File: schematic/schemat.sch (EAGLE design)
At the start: 69 parts, among them IC1 TB6612FNG, IC2 LM339D, IC3 7806DT, Q1 16MHz

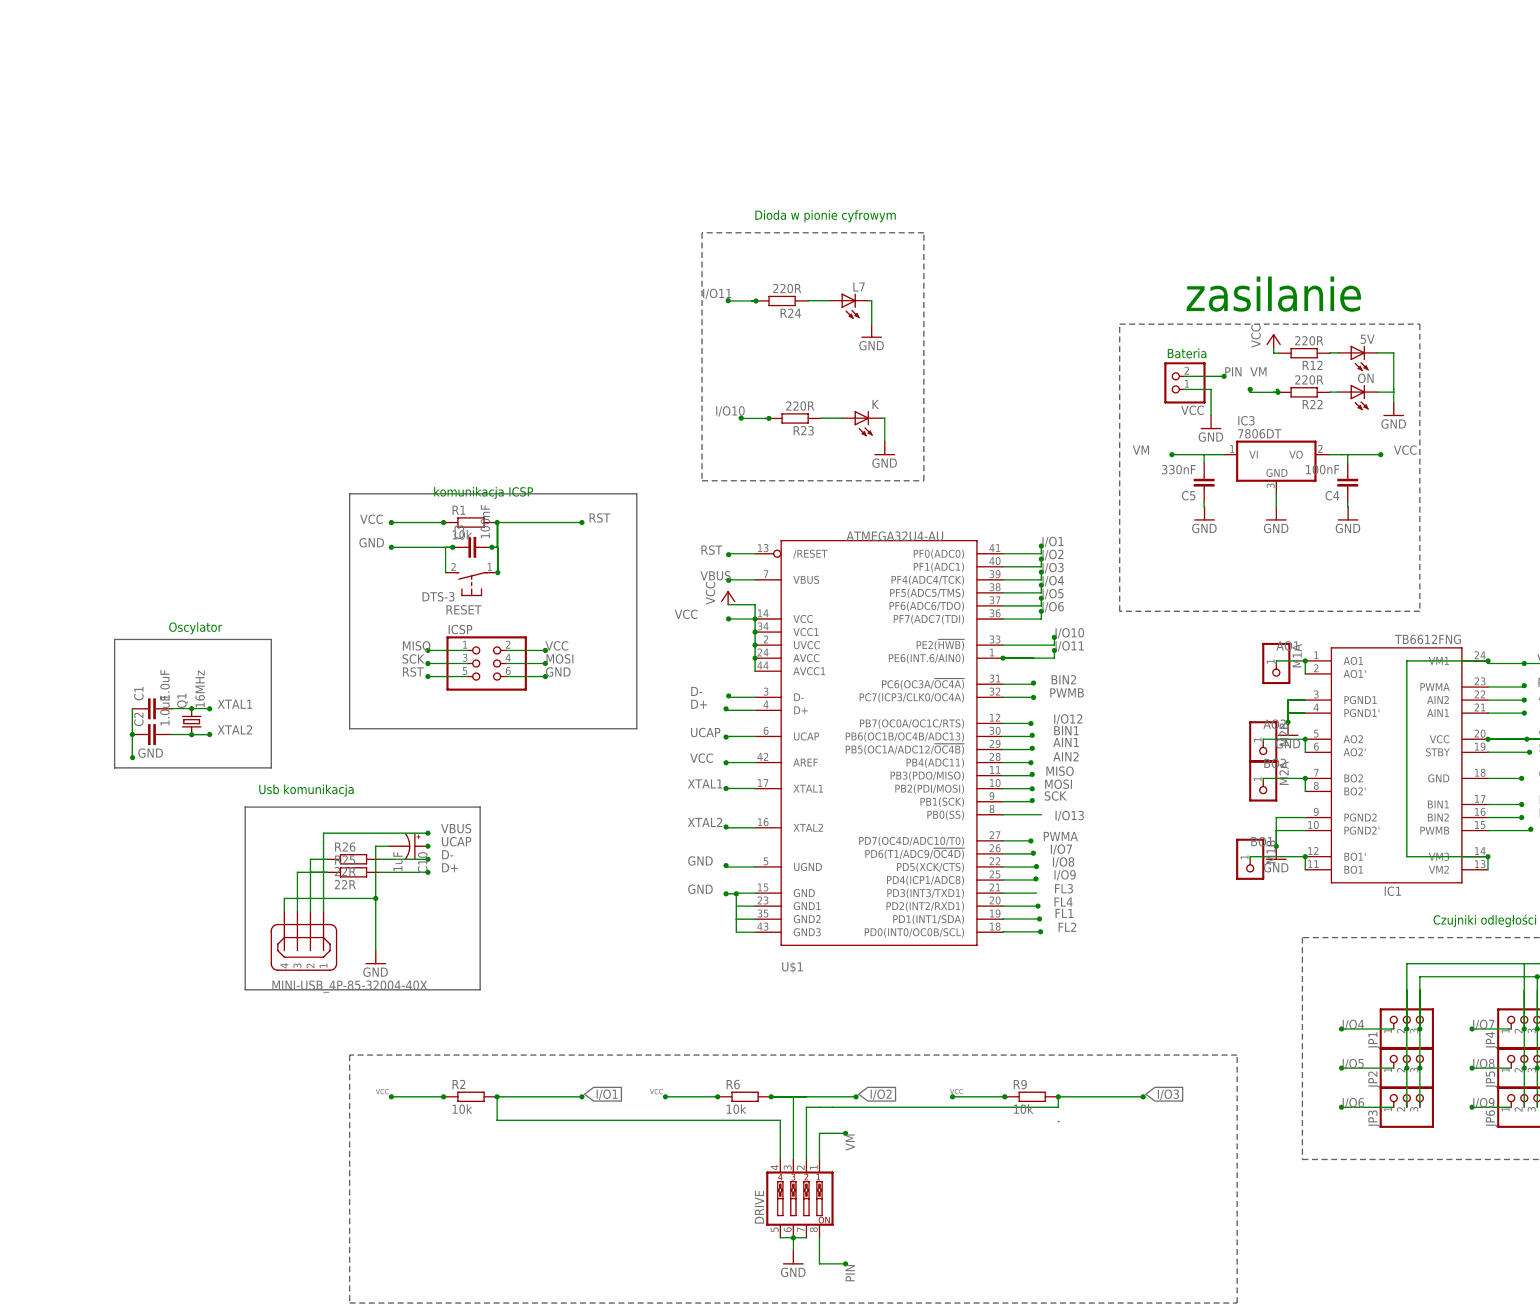
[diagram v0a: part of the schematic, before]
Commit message: poprawa wyglądu schematu
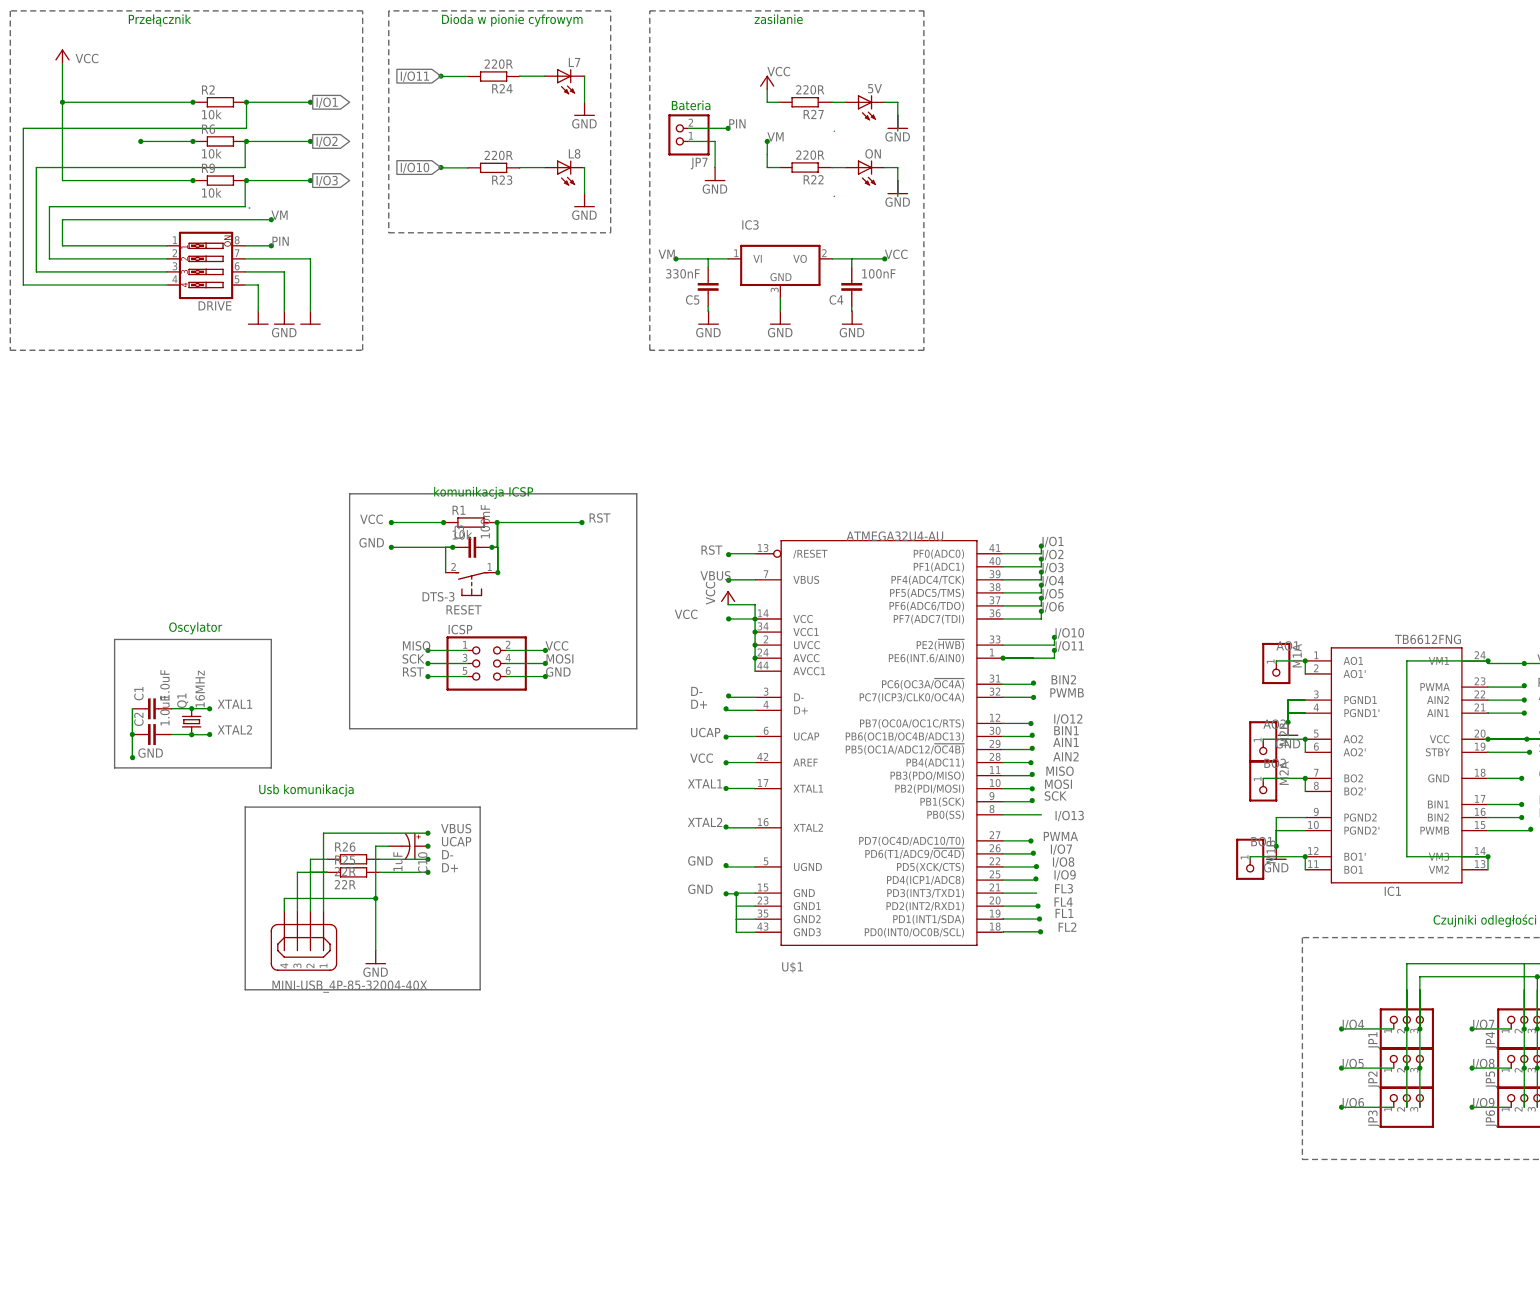
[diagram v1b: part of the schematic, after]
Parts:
- removed K: (no value), led:LEDCHIP-LED0805
- removed R12: 220R, rcl:R-EU_R0805
- removed VCC: (no value), pinhead:PINHD-1X2
- added JP7: (no value), pinhead:PINHD-1X2
- added L8: (no value), led:LEDCHIP-LED0805
- added R27: 220R, rcl:R-EU_R0805
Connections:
- new net N$34: R22.2
- net GND: now also JP7.1, L8.C; no longer K.C, VCC.1
- net N$2: now also L8.A; no longer K.A
- net N$7: now also R27.1; no longer R12.1
- net PIN: now also JP7.2; no longer VCC.2
- net VCC: now also R27.2; no longer R12.2
- net VM: no longer R22.2
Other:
- note added: "Przełącznik"
- moved on the sheet: 5V, C4, C5, DRIVE, IC3, L7, ON, R2, R22, R23, R24, R6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

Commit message: oscylatop + ISP
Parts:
- C1, C2: value 1.0uF -> 28pF
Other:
- note added: "oscylator"
- note removed: "Oscylator"
- moved on the sheet: C1, C2, C3, DRIVE, ICSP, Q1, R1, R2, R6, R9, RESET
